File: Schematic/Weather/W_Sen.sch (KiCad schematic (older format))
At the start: 27 parts, among them J8 3_Way_Wire, J9 3_Way_Wire, Q10 BSS138, Q11 AO3401, Q12 AO3401, U8 LM321

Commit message: more changes
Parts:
- renumbered C7 to C4, H13 to H15, H14 to H16, H15 to H17, H16 to H18, J8 to J21, J9 to J22, R45 to R43, R46 to R44, R47 to R45, R48 to R46, R49 to R47, R50 to R48, R51 to R49, R52 to R50, R53 to R51, R54 to R52, R55 to R53, R56 to R54, R57 to R55, R58 to R56, U8 to U7
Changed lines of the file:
@@
 $Descr A4 11693 8268
 encoding utf-8
-Sheet 13 14
+Sheet 13 15
 Title ""
 Date ""
@@
 P 5700 2150
 AR Path="/5C952539/5CB04490" Ref="U?"  Part="1"
-AR Path="/5CAC05F6/5CB04490" Ref="U8"  Part="1"
-F 0 "U8" H 5700 2631 50  0000 C CNN
+AR Path="/5CAC05F6/5CB04490" Ref="U7"  Part="1"
+F 0 "U7" H 5700 2631 50  0000 C CNN
 F 1 "LM321" H 5700 2540 50  0000 C CNN
 F 2 "Package_TO_SOT_SMD:SOT-23-5" H 5700 2150 50  0001 C CNN
@@
 P 5100 4800
 AR Path="/5C952539/5CB04496" Ref="R?"  Part="1"
-AR Path="/5CAC05F6/5CB04496" Ref="R45"  Part="1"
-F 0 "R45" V 4893 4800 50  0000 C CNN
+AR Path="/5CAC05F6/5CB04496" Ref="R43"  Part="1"
+F 0 "R43" V 4893 4800 50  0000 C CNN
 F 1 "2.2K" V 4984 4800 50  0000 C CNN
 F 2 "Resistor_THT:R_Axial_DIN0204_L3.6mm_D1.6mm_P2.54mm_Vertical" V 5030 4800 50  0001 C CNN
@@
 P 5500 5250
 AR Path="/5C952539/5CB0449C" Ref="R?"  Part="1"
-AR Path="/5CAC05F6/5CB0449C" Ref="R48"  Part="1"
-F 0 "R48" H 5430 5204 50  0000 R CNN
+AR Path="/5CAC05F6/5CB0449C" Ref="R46"  Part="1"
+F 0 "R46" H 5430 5204 50  0000 R CNN
 F 1 "5.1K" H 5430 5295 50  0000 R CNN
 F 2 "Resistor_THT:R_Axial_DIN0204_L3.6mm_D1.6mm_P2.54mm_Vertical" V 5430 5250 50  0001 C CNN
@@
 P 7000 4900
 AR Path="/5C952539/5CB044A2" Ref="R?"  Part="1"
-AR Path="/5CAC05F6/5CB044A2" Ref="R56"  Part="1"
-F 0 "R56" H 7070 4946 50  0000 L CNN
+AR Path="/5CAC05F6/5CB044A2" Ref="R54"  Part="1"
+F 0 "R54" H 7070 4946 50  0000 L CNN
 F 1 "680" H 7070 4855 50  0000 L CNN
 F 2 "Resistor_THT:R_Axial_DIN0204_L3.6mm_D1.6mm_P2.54mm_Vertical" V 6930 4900 50  0001 C CNN
@@
 P 6700 3900
 AR Path="/5C952539/5CB044A8" Ref="R?"  Part="1"
-AR Path="/5CAC05F6/5CB044A8" Ref="R54"  Part="1"
-F 0 "R54" H 6770 3946 50  0000 L CNN
+AR Path="/5CAC05F6/5CB044A8" Ref="R52"  Part="1"
+F 0 "R52" H 6770 3946 50  0000 L CNN
 F 1 "20K" H 6770 3855 50  0000 L CNN
 F 2 "Resistor_THT:R_Axial_DIN0204_L3.6mm_D1.6mm_P2.54mm_Vertical" V 6630 3900 50  0001 C CNN
@@
 P 5950 4150
 AR Path="/5C952539/5CB044AE" Ref="R?"  Part="1"
-AR Path="/5CAC05F6/5CB044AE" Ref="R50"  Part="1"
-F 0 "R50" H 6020 4196 50  0000 L CNN
+AR Path="/5CAC05F6/5CB044AE" Ref="R48"  Part="1"
+F 0 "R48" H 6020 4196 50  0000 L CNN
 F 1 "10K" H 6020 4105 50  0000 L CNN
 F 2 "Resistor_THT:R_Axial_DIN0204_L3.6mm_D1.6mm_P2.54mm_Vertical" V 5880 4150 50  0001 C CNN
@@
 P 5400 3700
 AR Path="/5C952539/5CB044B4" Ref="R?"  Part="1"
-AR Path="/5CAC05F6/5CB044B4" Ref="R47"  Part="1"
-F 0 "R47" H 5470 3746 50  0000 L CNN
+AR Path="/5CAC05F6/5CB044B4" Ref="R45"  Part="1"
+F 0 "R45" H 5470 3746 50  0000 L CNN
 F 1 "2.2k" H 5470 3655 50  0000 L CNN
 F 2 "Resistor_THT:R_Axial_DIN0204_L3.6mm_D1.6mm_P2.54mm_Vertical" V 5330 3700 50  0001 C CNN
@@
 P 6050 1700
 AR Path="/5C952539/5CB044BA" Ref="R?"  Part="1"
-AR Path="/5CAC05F6/5CB044BA" Ref="R51"  Part="1"
-F 0 "R51" H 6120 1746 50  0000 L CNN
+AR Path="/5CAC05F6/5CB044BA" Ref="R49"  Part="1"
+F 0 "R49" H 6120 1746 50  0000 L CNN
 F 1 "4.7K" H 6120 1655 50  0000 L CNN
 F 2 "Resistor_THT:R_Axial_DIN0204_L3.6mm_D1.6mm_P2.54mm_Vertical" V 5980 1700 50  0001 C CNN
@@
 P 5150 2150
 AR Path="/5C952539/5CB044CC" Ref="R?"  Part="1"
-AR Path="/5CAC05F6/5CB044CC" Ref="R46"  Part="1"
-F 0 "R46" V 4943 2150 50  0000 C CNN
+AR Path="/5CAC05F6/5CB044CC" Ref="R44"  Part="1"
+F 0 "R44" V 4943 2150 50  0000 C CNN
 F 1 "4.7K" V 5034 2150 50  0000 C CNN
 F 2 "Resistor_THT:R_Axial_DIN0204_L3.6mm_D1.6mm_P2.54mm_Vertical" V 5080 2150 50  0001 C CNN
@@
 P 6700 4900
 AR Path="/5C952539/5CB044EC" Ref="R?"  Part="1"
-AR Path="/5CAC05F6/5CB044EC" Ref="R55"  Part="1"
-F 0 "R55" H 6770 4946 50  0000 L CNN
+AR Path="/5CAC05F6/5CB044EC" Ref="R53"  Part="1"
+F 0 "R53" H 6770 4946 50  0000 L CNN
 F 1 "20K" H 6770 4855 50  0000 L CNN
 F 2 "Resistor_THT:R_Axial_DIN0204_L3.6mm_D1.6mm_P2.54mm_Vertical" V 6630 4900 50  0001 C CNN
@@
 P 7400 2250
 AR Path="/5C952539/5CB044FC" Ref="R?"  Part="1"
-AR Path="/5CAC05F6/5CB044FC" Ref="R58"  Part="1"
-F 0 "R58" V 7193 2250 50  0000 C CNN
+AR Path="/5CAC05F6/5CB044FC" Ref="R56"  Part="1"
+F 0 "R56" V 7193 2250 50  0000 C CNN
 F 1 "3.3k" V 7284 2250 50  0000 C CNN
 F 2 "Resistor_THT:R_Axial_DIN0204_L3.6mm_D1.6mm_P2.54mm_Vertical" V 7330 2250 50  0001 C CNN
@@
 P 6050 2650
 AR Path="/5C952539/5CB04503" Ref="R?"  Part="1"
-AR Path="/5CAC05F6/5CB04503" Ref="R52"  Part="1"
-F 0 "R52" H 6120 2696 50  0000 L CNN
+AR Path="/5CAC05F6/5CB04503" Ref="R50"  Part="1"
+F 0 "R50" H 6120 2696 50  0000 L CNN
 F 1 "4.7K" H 6120 2605 50  0000 L CNN
 F 2 "Resistor_THT:R_Axial_DIN0204_L3.6mm_D1.6mm_P2.54mm_Vertical" V 5980 2650 50  0001 C CNN
@@
 P 6550 2250
 AR Path="/5C952539/5CB0451F" Ref="C?"  Part="1"
-AR Path="/5CAC05F6/5CB0451F" Ref="C7"  Part="1"
-F 0 "C7" V 6298 2250 50  0000 C CNN
+AR Path="/5CAC05F6/5CB0451F" Ref="C4"  Part="1"
+F 0 "C4" V 6298 2250 50  0000 C CNN
 F 1 "0.1uF" V 6389 2250 50  0000 C CNN
 F 2 "Capacitor_THT:C_Disc_D3.8mm_W2.6mm_P2.50mm" H 6588 2100 50  0001 C CNN
@@
 P 6250 2250
 AR Path="/5C952539/5CB04529" Ref="R?"  Part="1"
-AR Path="/5CAC05F6/5CB04529" Ref="R53"  Part="1"
-F 0 "R53" V 6043 2250 50  0000 C CNN
+AR Path="/5CAC05F6/5CB04529" Ref="R51"  Part="1"
+F 0 "R51" V 6043 2250 50  0000 C CNN
 F 1 "4.7K" V 6134 2250 50  0000 C CNN
 F 2 "Resistor_THT:R_Axial_DIN0204_L3.6mm_D1.6mm_P2.54mm_Vertical" V 6180 2250 50  0001 C CNN
@@
 P 5550 2500
 AR Path="/5C952539/5CB04535" Ref="R?"  Part="1"
-AR Path="/5CAC05F6/5CB04535" Ref="R49"  Part="1"
-F 0 "R49" V 5343 2500 50  0000 C CNN
+AR Path="/5CAC05F6/5CB04535" Ref="R47"  Part="1"
+F 0 "R47" V 5343 2500 50  0000 C CNN
 F 1 "4.7K" V 5434 2500 50  0000 C CNN
 F 2 "Resistor_THT:R_Axial_DIN0204_L3.6mm_D1.6mm_P2.54mm_Vertical" V 5480 2500 50  0001 C CNN
@@
 P 7350 3800
 AR Path="/5C952539/5CB04550" Ref="R?"  Part="1"
-AR Path="/5CAC05F6/5CB04550" Ref="R57"  Part="1"
-F 0 "R57" H 7420 3846 50  0000 L CNN
+AR Path="/5CAC05F6/5CB04550" Ref="R55"  Part="1"
+F 0 "R55" H 7420 3846 50  0000 L CNN
 F 1 "47K" H 7420 3755 50  0000 L CNN
 F 2 "Resistor_THT:R_Axial_DIN0204_L3.6mm_D1.6mm_P2.54mm_Vertical" V 7280 3800 50  0001 C CNN
@@
 P 3300 2000
 AR Path="/5C952539/5CB0455E" Ref="J?"  Part="1"
-AR Path="/5CAC05F6/5CB0455E" Ref="J9"  Part="1"
-F 0 "J9" H 3150 1600 50  0000 L CNN
+AR Path="/5CAC05F6/5CB0455E" Ref="J22"  Part="1"
+F 0 "J22" H 3150 1600 50  0000 L CNN
 F 1 "3_Way_Wire" H 3100 1450 50  0000 L CNN
 F 2 "Connector_PinHeader_2.54mm:PinHeader_1x03_P2.54mm_Vertical" H 3300 2000 50  0001 C CNN
@@
 P 3250 3350
 AR Path="/5C952539/5CB04569" Ref="J?"  Part="1"
-AR Path="/5CAC05F6/5CB04569" Ref="J8"  Part="1"
-F 0 "J8" H 3150 2950 50  0000 L CNN
+AR Path="/5CAC05F6/5CB04569" Ref="J21"  Part="1"
+F 0 "J21" H 3150 2950 50  0000 L CNN
 F 1 "3_Way_Wire" H 3100 2800 50  0000 L CNN
 F 2 "Connector_PinHeader_2.54mm:PinHeader_1x03_P2.54mm_Vertical" H 3250 3350 50  0001 C CNN
@@
 P 8000 3350
 AR Path="/5C952539/5CB04582" Ref="H?"  Part="1"
-AR Path="/5CAC05F6/5CB04582" Ref="H13"  Part="1"
-F 0 "H13" H 8100 3399 50  0000 L CNN
+AR Path="/5CAC05F6/5CB04582" Ref="H15"  Part="1"
+F 0 "H15" H 8100 3399 50  0000 L CNN
 F 1 "MountingHole_Pad" H 8100 3308 50  0000 L CNN
 F 2 "Connector_Wire:SolderWirePad_1x01_Drill0.8mm" H 8000 3350 50  0001 C CNN
@@
 P 8000 3850
 AR Path="/5C952539/5CB04588" Ref="H?"  Part="1"
-AR Path="/5CAC05F6/5CB04588" Ref="H15"  Part="1"
-F 0 "H15" H 8100 3899 50  0000 L CNN
+AR Path="/5CAC05F6/5CB04588" Ref="H17"  Part="1"
+F 0 "H17" H 8100 3899 50  0000 L CNN
 F 1 "MountingHole_Pad" H 8100 3808 50  0000 L CNN
 F 2 "Connector_Wire:SolderWirePad_1x01_Drill0.8mm" H 8000 3850 50  0001 C CNN
@@
 P 8000 3550
 AR Path="/5C952539/5CB0458E" Ref="H?"  Part="1"
-AR Path="/5CAC05F6/5CB0458E" Ref="H14"  Part="1"
-F 0 "H14" H 7900 3507 50  0000 R CNN
+AR Path="/5CAC05F6/5CB0458E" Ref="H16"  Part="1"
+F 0 "H16" H 7900 3507 50  0000 R CNN
 F 1 "MountingHole_Pad" H 7900 3598 50  0000 R CNN
 F 2 "Connector_Wire:SolderWirePad_1x01_Drill0.8mm" H 8000 3550 50  0001 C CNN
@@
 P 8000 4050
 AR Path="/5C952539/5CB04595" Ref="H?"  Part="1"
-AR Path="/5CAC05F6/5CB04595" Ref="H16"  Part="1"
-F 0 "H16" H 7900 4007 50  0000 R CNN
+AR Path="/5CAC05F6/5CB04595" Ref="H18"  Part="1"
+F 0 "H18" H 7900 4007 50  0000 R CNN
 F 1 "MountingHole_Pad" H 7900 4098 50  0000 R CNN
 F 2 "Connector_Wire:SolderWirePad_1x01_Drill0.8mm" H 8000 4050 50  0001 C CNN

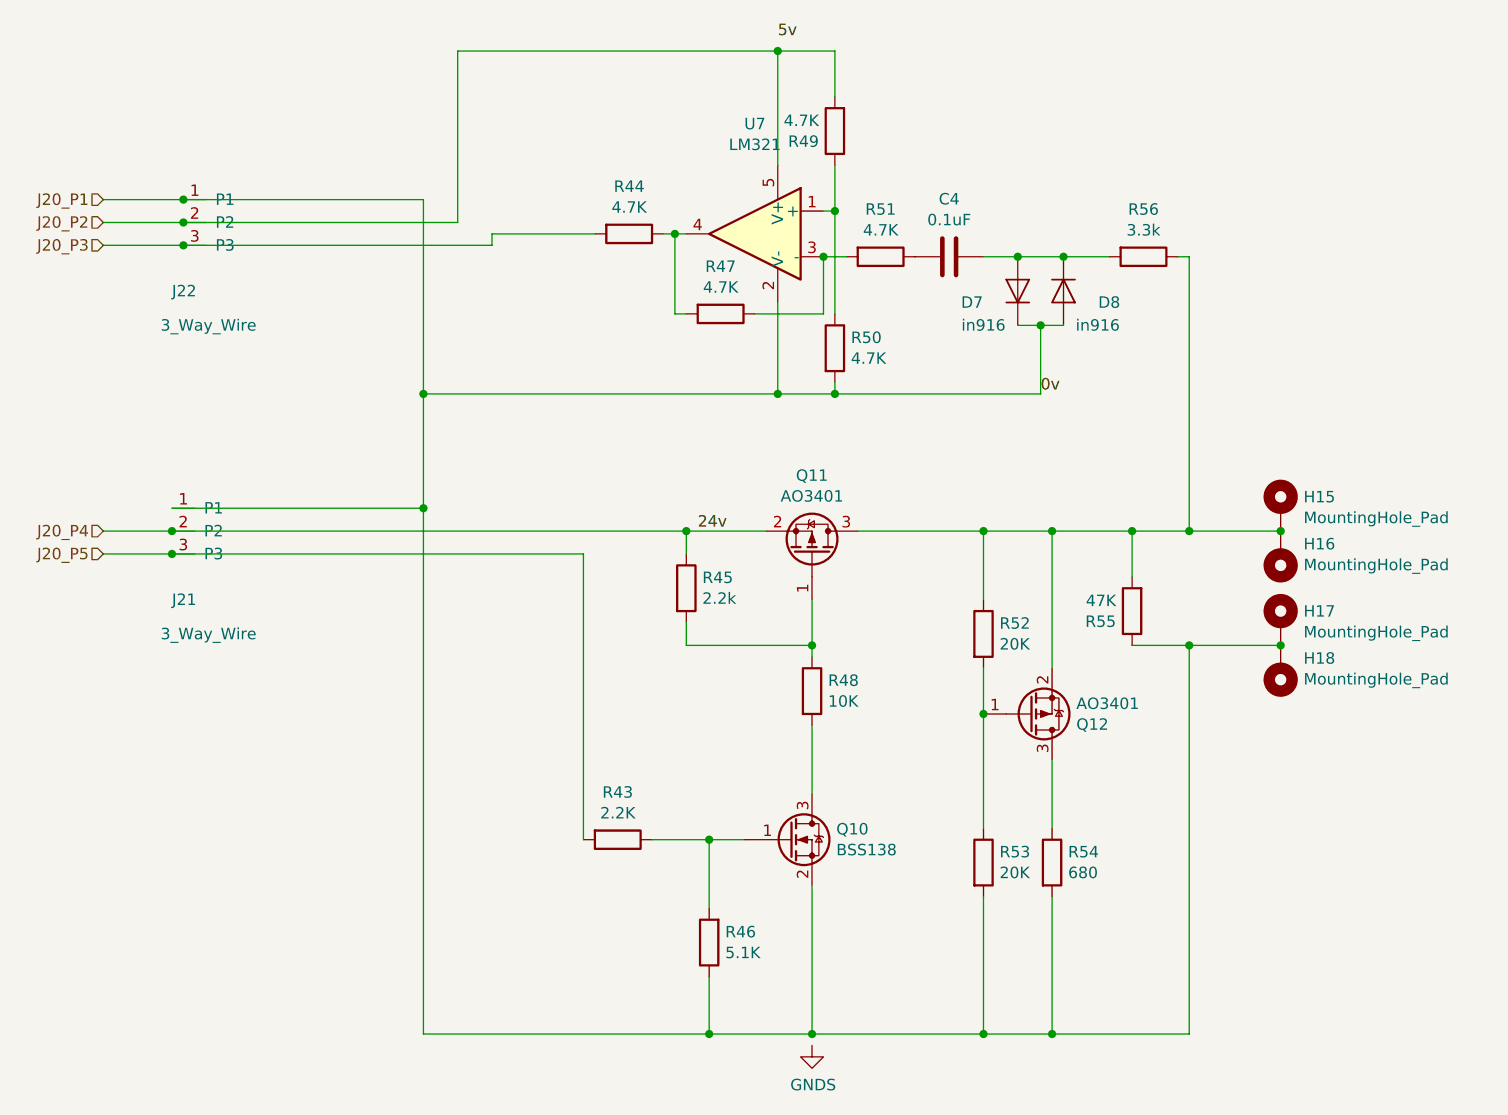
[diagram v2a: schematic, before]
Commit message: Connector relable start
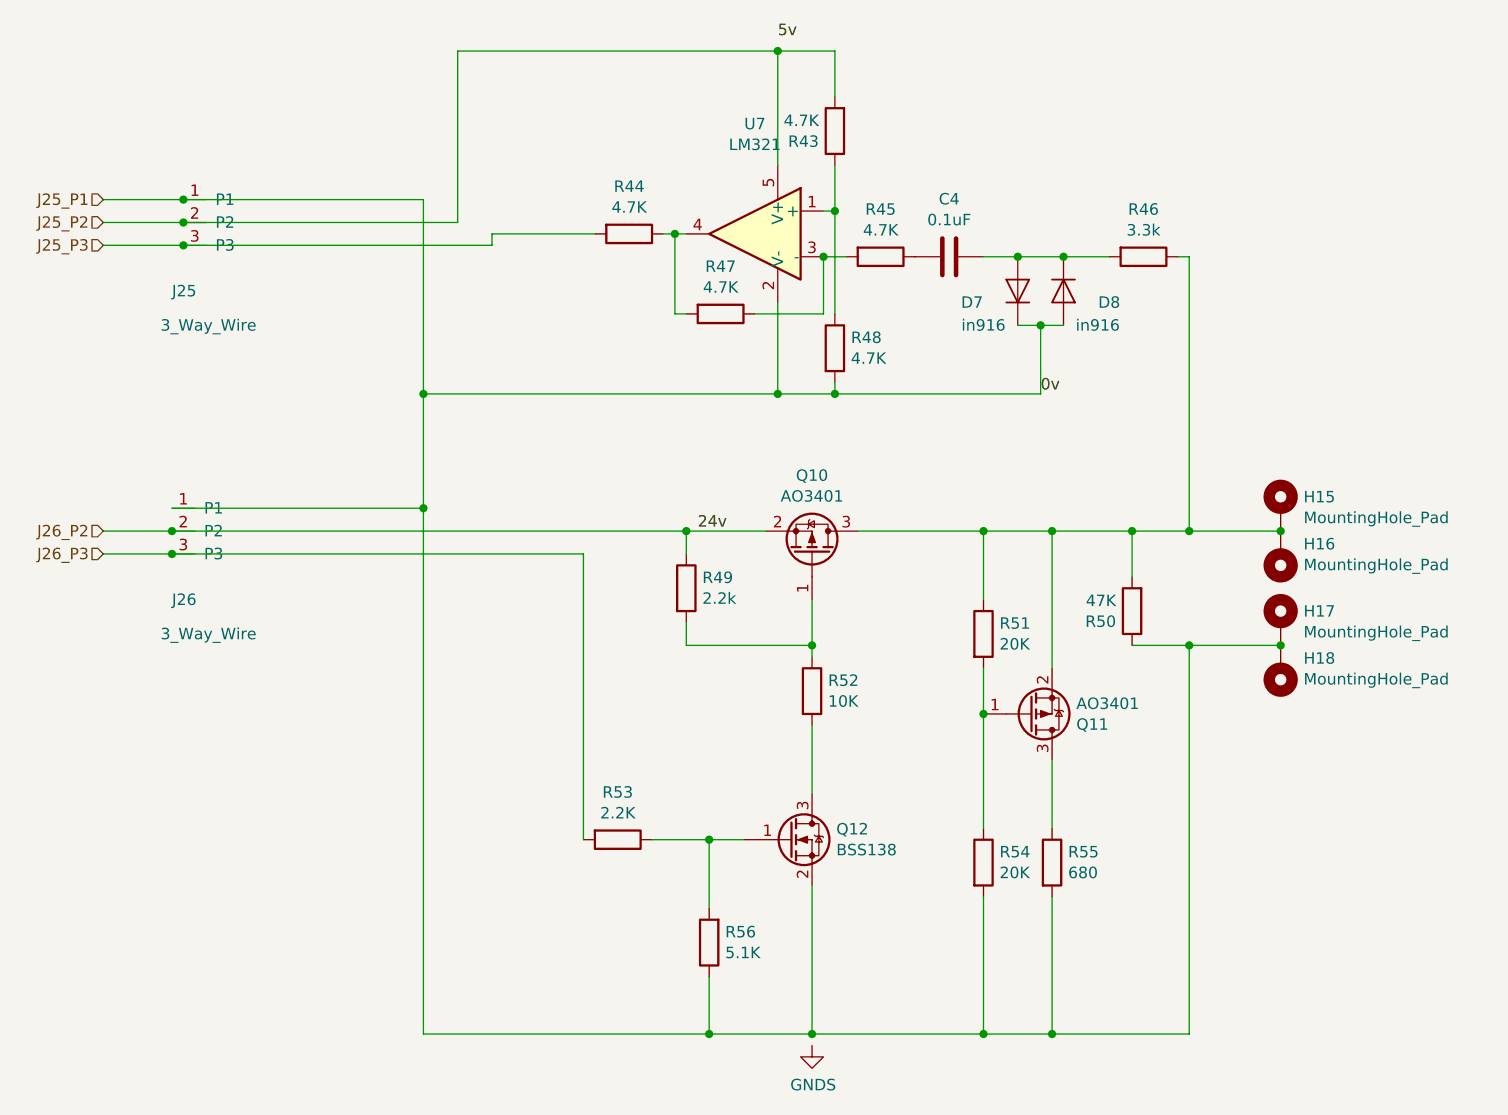
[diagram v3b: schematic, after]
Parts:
- renumbered J22 to J25, J21 to J26, Q11 to Q10, Q12 to Q11, Q10 to Q12, R49 to R43, R51 to R45, R56 to R46, R50 to R48, R45 to R49, R55 to R50, R52 to R51, R48 to R52, R43 to R53, R53 to R54, R54 to R55, R46 to R56
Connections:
- net J20_P1 renamed J25_P1
- net J20_P2 renamed J25_P2
- net J20_P3 renamed J25_P3
- net J20_P4 renamed J26_P2
- net J20_P5 renamed J26_P3
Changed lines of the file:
@@
 $Descr A4 11693 8268
 encoding utf-8
-Sheet 13 15
+Sheet 10 15
 Title ""
 Date ""
@@
 $EndDescr
 Text HLabel 2850 2000 0    50   Input ~ 0
-J20_P1
+J25_P1
 Text HLabel 2850 2100 0    50   Input ~ 0
-J20_P2
+J25_P2
 Text HLabel 2850 2200 0    50   Input ~ 0
-J20_P3
+J25_P3
 Text HLabel 2850 3450 0    50   Input ~ 0
-J20_P4
+J26_P2
 $Comp
 L Weather-rescue:AO3401-Transistor_FET Q?
@@
 P 5950 3550
 AR Path="/5C952539/5CB04484" Ref="Q?"  Part="1"
-AR Path="/5CAC05F6/5CB04484" Ref="Q11"  Part="1"
-F 0 "Q11" V 6293 3550 50  0000 C CNN
+AR Path="/5CAC05F6/5CB04484" Ref="Q10"  Part="1"
+F 0 "Q10" V 6293 3550 50  0000 C CNN
 F 1 "AO3401" V 6202 3550 50  0000 C CNN
 F 2 "Package_TO_SOT_SMD:SOT-23" H 6150 3475 50  0001 L CIN
@@
 P 5850 4800
 AR Path="/5C952539/5CB0448A" Ref="Q?"  Part="1"
-AR Path="/5CAC05F6/5CB0448A" Ref="Q10"  Part="1"
-F 0 "Q10" H 6056 4846 50  0000 L CNN
+AR Path="/5CAC05F6/5CB0448A" Ref="Q12"  Part="1"
+F 0 "Q12" H 6056 4846 50  0000 L CNN
 F 1 "BSS138" H 6056 4755 50  0000 L CNN
 F 2 "Package_TO_SOT_SMD:SOT-23" H 6050 4725 50  0001 L CIN
@@
 P 5100 4800
 AR Path="/5C952539/5CB04496" Ref="R?"  Part="1"
-AR Path="/5CAC05F6/5CB04496" Ref="R43"  Part="1"
-F 0 "R43" V 4893 4800 50  0000 C CNN
+AR Path="/5CAC05F6/5CB04496" Ref="R53"  Part="1"
+F 0 "R53" V 4893 4800 50  0000 C CNN
 F 1 "2.2K" V 4984 4800 50  0000 C CNN
 F 2 "Resistor_THT:R_Axial_DIN0204_L3.6mm_D1.6mm_P2.54mm_Vertical" V 5030 4800 50  0001 C CNN
@@
 P 5500 5250
 AR Path="/5C952539/5CB0449C" Ref="R?"  Part="1"
-AR Path="/5CAC05F6/5CB0449C" Ref="R46"  Part="1"
-F 0 "R46" H 5430 5204 50  0000 R CNN
+AR Path="/5CAC05F6/5CB0449C" Ref="R56"  Part="1"
+F 0 "R56" H 5430 5204 50  0000 R CNN
 F 1 "5.1K" H 5430 5295 50  0000 R CNN
 F 2 "Resistor_THT:R_Axial_DIN0204_L3.6mm_D1.6mm_P2.54mm_Vertical" V 5430 5250 50  0001 C CNN
@@
 P 7000 4900
 AR Path="/5C952539/5CB044A2" Ref="R?"  Part="1"
-AR Path="/5CAC05F6/5CB044A2" Ref="R54"  Part="1"
-F 0 "R54" H 7070 4946 50  0000 L CNN
+AR Path="/5CAC05F6/5CB044A2" Ref="R55"  Part="1"
+F 0 "R55" H 7070 4946 50  0000 L CNN
 F 1 "680" H 7070 4855 50  0000 L CNN
 F 2 "Resistor_THT:R_Axial_DIN0204_L3.6mm_D1.6mm_P2.54mm_Vertical" V 6930 4900 50  0001 C CNN
@@
 P 6700 3900
 AR Path="/5C952539/5CB044A8" Ref="R?"  Part="1"
-AR Path="/5CAC05F6/5CB044A8" Ref="R52"  Part="1"
-F 0 "R52" H 6770 3946 50  0000 L CNN
+AR Path="/5CAC05F6/5CB044A8" Ref="R51"  Part="1"
+F 0 "R51" H 6770 3946 50  0000 L CNN
 F 1 "20K" H 6770 3855 50  0000 L CNN
 F 2 "Resistor_THT:R_Axial_DIN0204_L3.6mm_D1.6mm_P2.54mm_Vertical" V 6630 3900 50  0001 C CNN
@@
 P 5950 4150
 AR Path="/5C952539/5CB044AE" Ref="R?"  Part="1"
-AR Path="/5CAC05F6/5CB044AE" Ref="R48"  Part="1"
-F 0 "R48" H 6020 4196 50  0000 L CNN
+AR Path="/5CAC05F6/5CB044AE" Ref="R52"  Part="1"
+F 0 "R52" H 6020 4196 50  0000 L CNN
 F 1 "10K" H 6020 4105 50  0000 L CNN
 F 2 "Resistor_THT:R_Axial_DIN0204_L3.6mm_D1.6mm_P2.54mm_Vertical" V 5880 4150 50  0001 C CNN
@@
 P 5400 3700
 AR Path="/5C952539/5CB044B4" Ref="R?"  Part="1"
-AR Path="/5CAC05F6/5CB044B4" Ref="R45"  Part="1"
-F 0 "R45" H 5470 3746 50  0000 L CNN
+AR Path="/5CAC05F6/5CB044B4" Ref="R49"  Part="1"
+F 0 "R49" H 5470 3746 50  0000 L CNN
 F 1 "2.2k" H 5470 3655 50  0000 L CNN
 F 2 "Resistor_THT:R_Axial_DIN0204_L3.6mm_D1.6mm_P2.54mm_Vertical" V 5330 3700 50  0001 C CNN
@@
 P 6050 1700
 AR Path="/5C952539/5CB044BA" Ref="R?"  Part="1"
-AR Path="/5CAC05F6/5CB044BA" Ref="R49"  Part="1"
-F 0 "R49" H 6120 1746 50  0000 L CNN
+AR Path="/5CAC05F6/5CB044BA" Ref="R43"  Part="1"
+F 0 "R43" H 6120 1746 50  0000 L CNN
 F 1 "4.7K" H 6120 1655 50  0000 L CNN
 F 2 "Resistor_THT:R_Axial_DIN0204_L3.6mm_D1.6mm_P2.54mm_Vertical" V 5980 1700 50  0001 C CNN
@@
 P 6900 4250
 AR Path="/5C952539/5CB044E5" Ref="Q?"  Part="1"
-AR Path="/5CAC05F6/5CB044E5" Ref="Q12"  Part="1"
-F 0 "Q12" H 7106 4296 50  0000 L CNN
+AR Path="/5CAC05F6/5CB044E5" Ref="Q11"  Part="1"
+F 0 "Q11" H 7106 4296 50  0000 L CNN
 F 1 "AO3401" H 7106 4205 50  0000 L CNN
 F 2 "Package_TO_SOT_SMD:SOT-23" H 7100 4175 50  0001 L CIN
@@
 P 6700 4900
 AR Path="/5C952539/5CB044EC" Ref="R?"  Part="1"
-AR Path="/5CAC05F6/5CB044EC" Ref="R53"  Part="1"
-F 0 "R53" H 6770 4946 50  0000 L CNN
+AR Path="/5CAC05F6/5CB044EC" Ref="R54"  Part="1"
+F 0 "R54" H 6770 4946 50  0000 L CNN
 F 1 "20K" H 6770 4855 50  0000 L CNN
 F 2 "Resistor_THT:R_Axial_DIN0204_L3.6mm_D1.6mm_P2.54mm_Vertical" V 6630 4900 50  0001 C CNN
@@
 P 7400 2250
 AR Path="/5C952539/5CB044FC" Ref="R?"  Part="1"
-AR Path="/5CAC05F6/5CB044FC" Ref="R56"  Part="1"
-F 0 "R56" V 7193 2250 50  0000 C CNN
+AR Path="/5CAC05F6/5CB044FC" Ref="R46"  Part="1"
+F 0 "R46" V 7193 2250 50  0000 C CNN
 F 1 "3.3k" V 7284 2250 50  0000 C CNN
 F 2 "Resistor_THT:R_Axial_DIN0204_L3.6mm_D1.6mm_P2.54mm_Vertical" V 7330 2250 50  0001 C CNN
@@
 P 6050 2650
 AR Path="/5C952539/5CB04503" Ref="R?"  Part="1"
-AR Path="/5CAC05F6/5CB04503" Ref="R50"  Part="1"
-F 0 "R50" H 6120 2696 50  0000 L CNN
+AR Path="/5CAC05F6/5CB04503" Ref="R48"  Part="1"
+F 0 "R48" H 6120 2696 50  0000 L CNN
 F 1 "4.7K" H 6120 2605 50  0000 L CNN
 F 2 "Resistor_THT:R_Axial_DIN0204_L3.6mm_D1.6mm_P2.54mm_Vertical" V 5980 2650 50  0001 C CNN
@@
 P 6250 2250
 AR Path="/5C952539/5CB04529" Ref="R?"  Part="1"
-AR Path="/5CAC05F6/5CB04529" Ref="R51"  Part="1"
-F 0 "R51" V 6043 2250 50  0000 C CNN
+AR Path="/5CAC05F6/5CB04529" Ref="R45"  Part="1"
+F 0 "R45" V 6043 2250 50  0000 C CNN
 F 1 "4.7K" V 6134 2250 50  0000 C CNN
 F 2 "Resistor_THT:R_Axial_DIN0204_L3.6mm_D1.6mm_P2.54mm_Vertical" V 6180 2250 50  0001 C CNN
@@
 Connection ~ 6000 2250
 Text HLabel 2850 3550 0    50   Input ~ 0
-J20_P5
+J26_P3
 Wire Wire Line
 	5400 3850 5400 3950
@@
 P 7350 3800
 AR Path="/5C952539/5CB04550" Ref="R?"  Part="1"
-AR Path="/5CAC05F6/5CB04550" Ref="R55"  Part="1"
-F 0 "R55" H 7420 3846 50  0000 L CNN
+AR Path="/5CAC05F6/5CB04550" Ref="R50"  Part="1"
+F 0 "R50" H 7420 3846 50  0000 L CNN
 F 1 "47K" H 7420 3755 50  0000 L CNN
 F 2 "Resistor_THT:R_Axial_DIN0204_L3.6mm_D1.6mm_P2.54mm_Vertical" V 7280 3800 50  0001 C CNN
@@
 P 3300 2000
 AR Path="/5C952539/5CB0455E" Ref="J?"  Part="1"
-AR Path="/5CAC05F6/5CB0455E" Ref="J22"  Part="1"
-F 0 "J22" H 3150 1600 50  0000 L CNN
+AR Path="/5CAC05F6/5CB0455E" Ref="J25"  Part="1"
+F 0 "J25" H 3150 1600 50  0000 L CNN
 F 1 "3_Way_Wire" H 3100 1450 50  0000 L CNN
 F 2 "Connector_PinHeader_2.54mm:PinHeader_1x03_P2.54mm_Vertical" H 3300 2000 50  0001 C CNN
@@
 P 3250 3350
 AR Path="/5C952539/5CB04569" Ref="J?"  Part="1"
-AR Path="/5CAC05F6/5CB04569" Ref="J21"  Part="1"
-F 0 "J21" H 3150 2950 50  0000 L CNN
+AR Path="/5CAC05F6/5CB04569" Ref="J26"  Part="1"
+F 0 "J26" H 3150 2950 50  0000 L CNN
 F 1 "3_Way_Wire" H 3100 2800 50  0000 L CNN
 F 2 "Connector_PinHeader_2.54mm:PinHeader_1x03_P2.54mm_Vertical" H 3250 3350 50  0001 C CNN
